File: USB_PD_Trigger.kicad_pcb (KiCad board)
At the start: 2 copper layers, 54.4 x 31.6 mm, 54 parts, among them J1 Conn_02x08_Odd_Even, J2 Conn_02x08_Odd_Even, J3 Conn_01x02, U1 AP33771C, U2 HP8KB7TB1, X1 2171790001, X2 Screw_Terminal_01x02

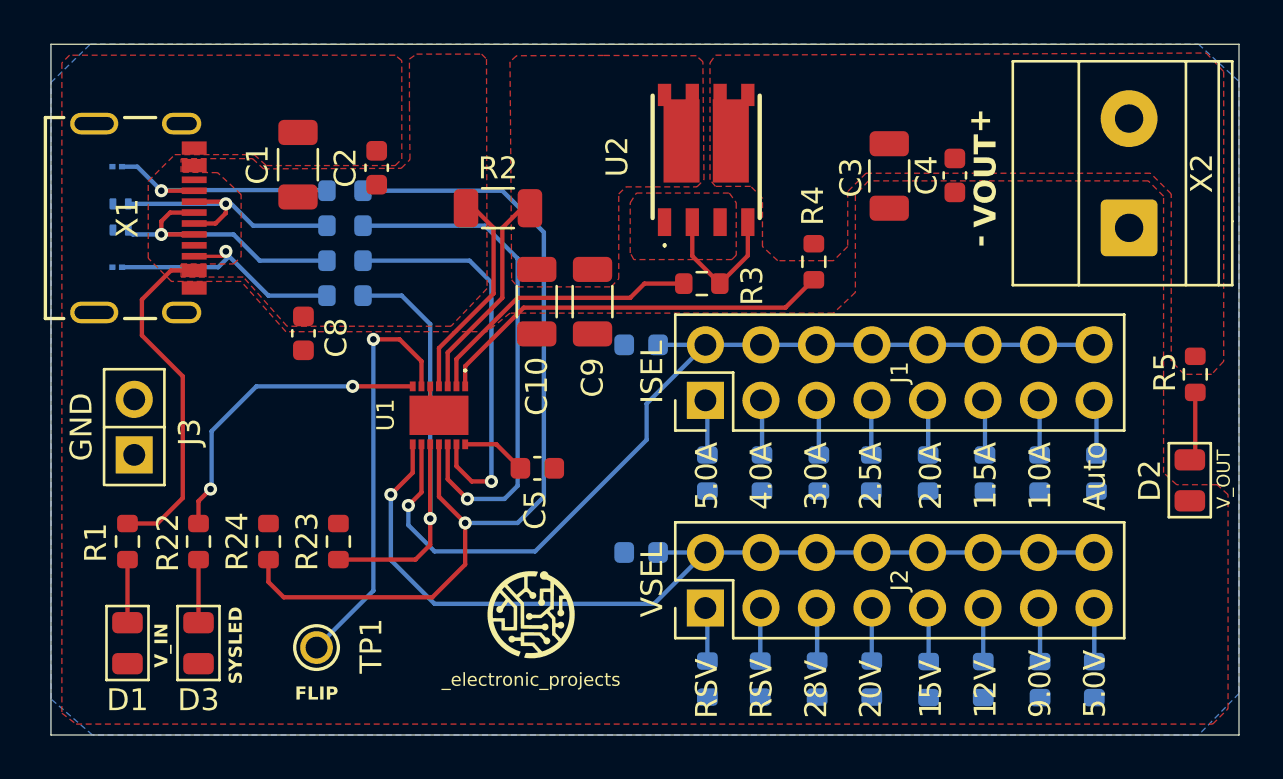
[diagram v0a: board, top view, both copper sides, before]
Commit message: added stitching vias and changed ESD diodes
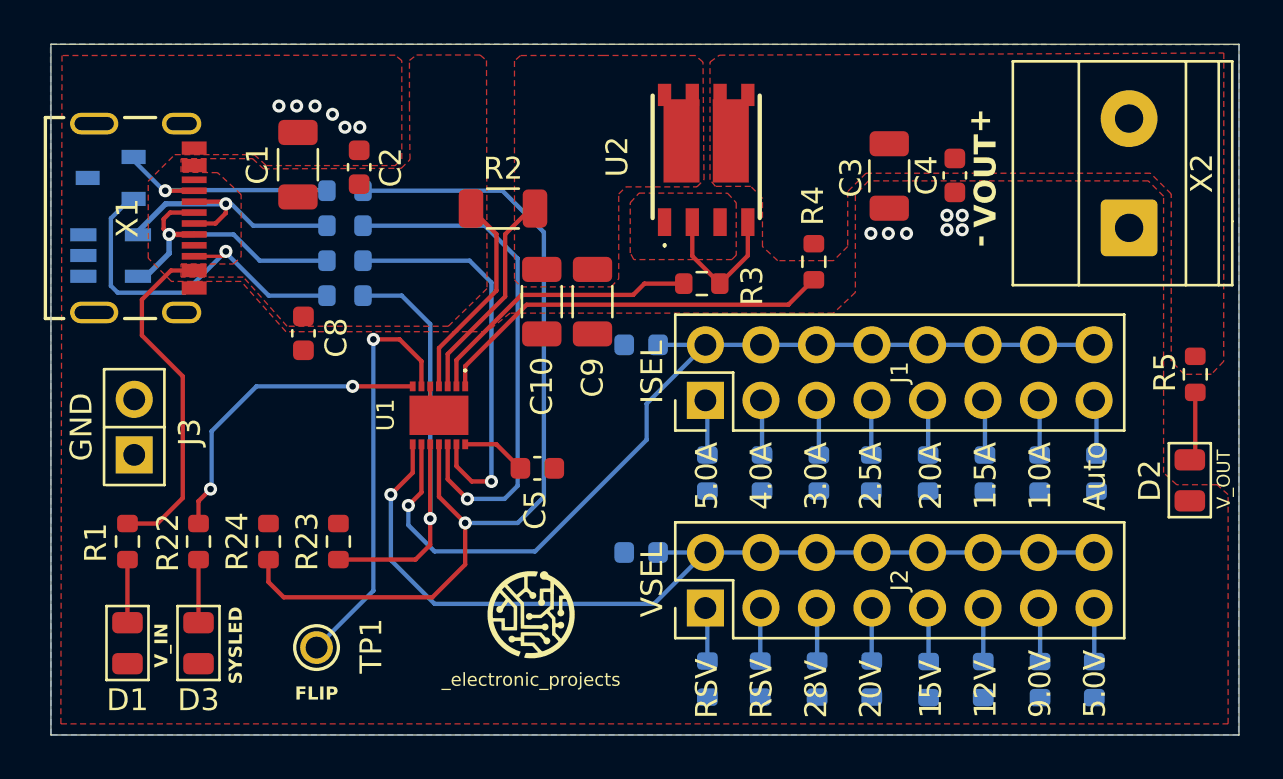
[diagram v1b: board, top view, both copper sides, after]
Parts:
- removed D6, D7: ESD321DPYR, footprints:ESD321DPYR
- D4: value ESD441DPLR -> SOT96P240X110-3N; footprint footprints:ESD441DPLR -> footprints:DT1452-02SO-7
- D5: value ESD441DPLR -> ESDS312DBVR; footprint footprints:ESD441DPLR -> footprints:ESDS312DBVR
- moved C2 0.80 mm to (138.9, 97.6)
- moved D5 0.61 mm to (127.5, 101.7), turned to 0 degrees
- moved D4 0.60 mm to (127.5, 98.1)
- moved R2 0.23 mm to (145.4, 99.5)
- moved C10 0.23 mm to (147.2, 103.8)
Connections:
- D4 pad 2: GND -> /CC2
- D5 pad 1: /CC2 -> GND
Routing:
- net /CC2: track 12.3 -> 17.8 mm
- net /DP: track 13.4 -> 14.1 mm
- net GND: vias 0 -> 13
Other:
- board text added: "AP33771C USB PD Trigger Board 20260115 v1.0"
- board text removed: "AP33771C USB PD Trigger Board 20260110 v1.0"
